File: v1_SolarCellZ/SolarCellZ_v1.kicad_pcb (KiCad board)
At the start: 6 copper layers, 48.4 x 48.4 mm, 58 parts, among them IC1 TSL2561, J1 XF2M-1015-1A, Q1 IRLML2803, U1 NDS8434, U2 Value

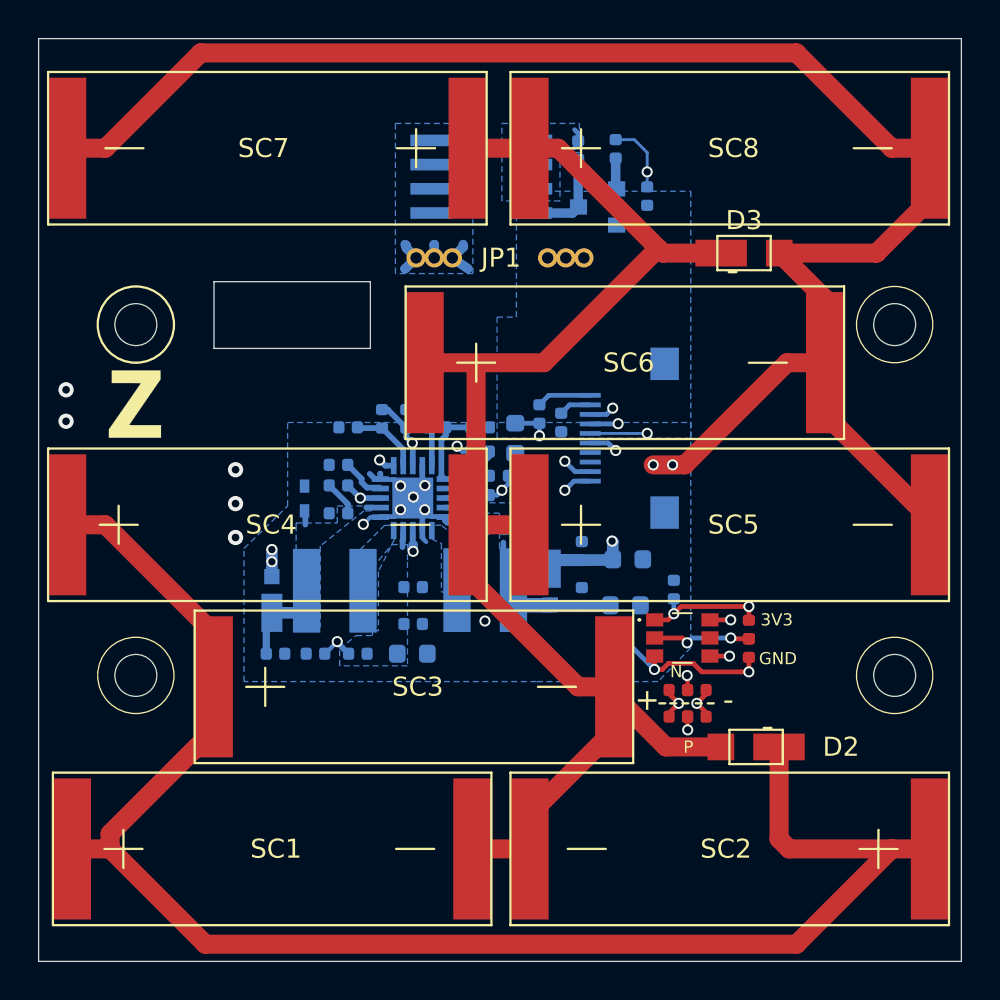
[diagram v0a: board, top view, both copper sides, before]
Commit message: Fixed floating via, extended pads, and added flatflex labels
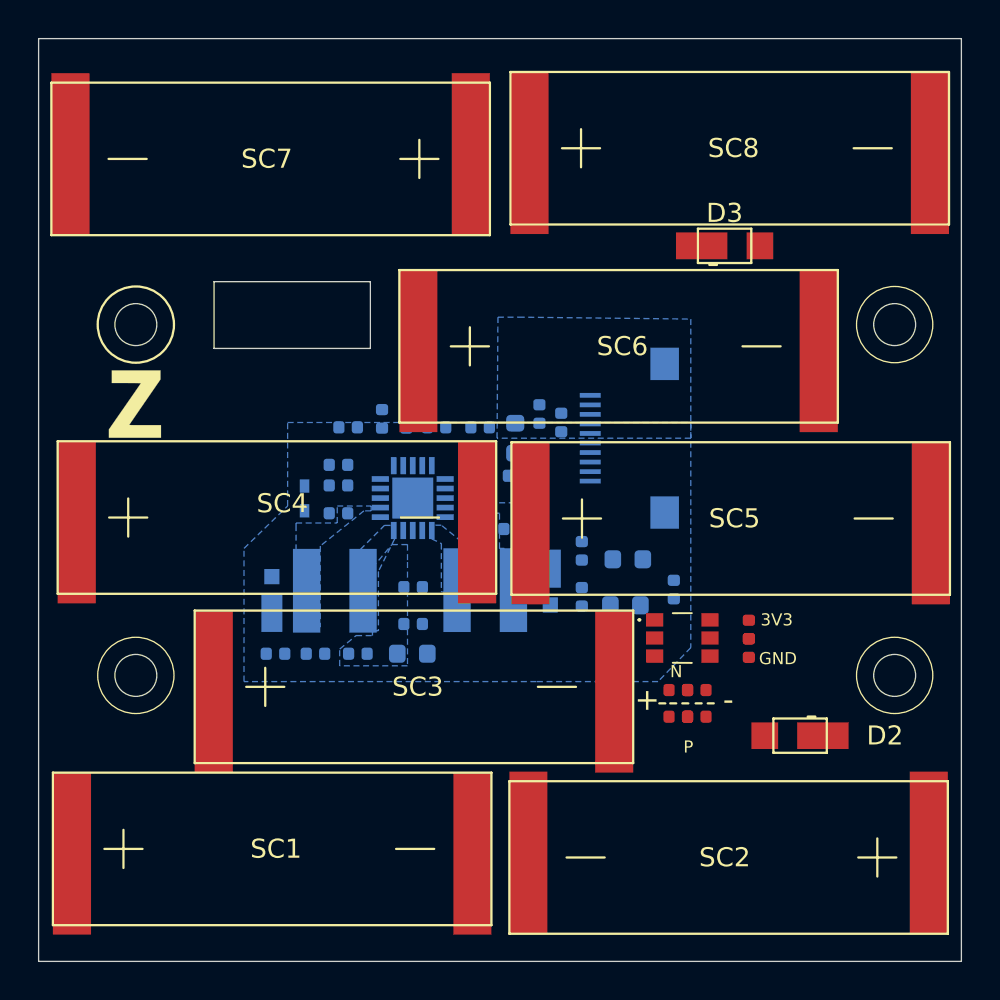
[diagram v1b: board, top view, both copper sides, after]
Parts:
- removed JP1: Jumper, SolarCellParts:Burn-Wire-Rotated
- removed Q1: IRLML2803, Package_TO_SOT_SMD:SOT-23
- removed the R3 at (121.9, 48.3)
- removed the R4 at (120.3, 45.8)
- removed the R5 at (118.3, 45.8)
- removed U1: NDS8434, custom-footprints:NDS8434
- moved D2 2.38 mm to (129.9, 76.6)
- moved D3 1.09 mm to (126.0, 50.9)
- moved SC6 0.92 mm to (109.9, 56.1)
- moved SC4 0.63 mm to (92.0, 65.1)
- moved SC7 0.59 mm to (112.7, 46.3)
- moved SC2 0.45 mm to (136.7, 83.0)
- moved SC5 0.33 mm to (115.8, 65.2)
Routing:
- net /coil: track 17213.2 -> 0.00 mm, vias 7 -> 0
- net GND: track 119.6 -> 0.00 mm, vias 11 -> 0
- net VSOLAR: track 92.9 -> 0.00 mm
- net Net-(D2-Pad2): track 72.0 -> 0.00 mm
- net +3V3: track 22.7 -> 0.00 mm, vias 4 -> 0
- net COIL_P: track 21.0 -> 0.00 mm, vias 2 -> 0
- net BURN1: track 20.4 -> 0.00 mm, vias 2 -> 0
- net SCL1: track 17.1 -> 0.00 mm, vias 2 -> 0
- net COIL_N: track 16.6 -> 0.00 mm, vias 2 -> 0
- net SDA1: track 16.3 -> 0.00 mm, vias 2 -> 0
- net /VBAT: track 13.9 -> 0.00 mm, vias 2 -> 0
- net Net-(R14-Pad1): track 11.8 -> 0.00 mm, vias 2 -> 0
- net VOUT_EN: track 9.60 -> 0.00 mm, vias 2 -> 0
- net Net-(C10-Pad1): track 9.20 -> 0.00 mm
- net Net-(R10-Pad2): track 7.04 -> 0.00 mm, vias 2 -> 0
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- removed copper zone on B.Cu, net /VBURN
- removed copper zone on B.Cu, net BATT_P
